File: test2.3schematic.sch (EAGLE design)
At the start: 24 parts, among them IC1 NCS21911SN2T1G, IC2 FXLN8371QR1, IC3 MAX25210ATAB9_V+, IC4 NCS21911SN2T1G, IC5 NCS21911SN2T1G

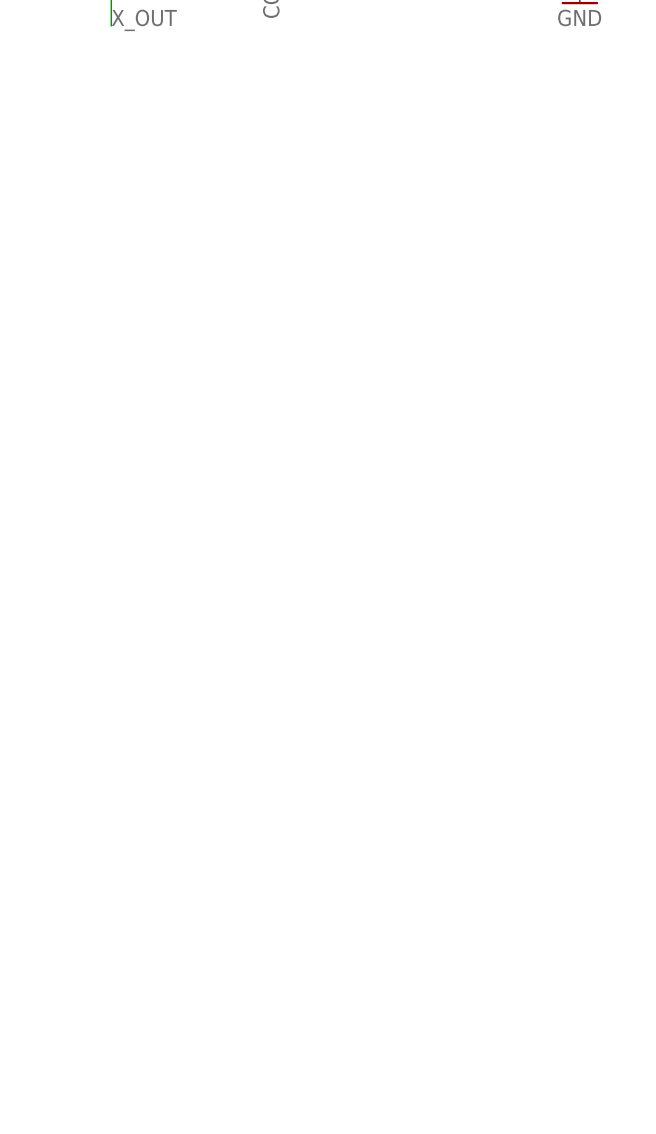
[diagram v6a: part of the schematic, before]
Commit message: FInal PCB, some parts might be bought using diff website if not PCB will be revised for later deadline
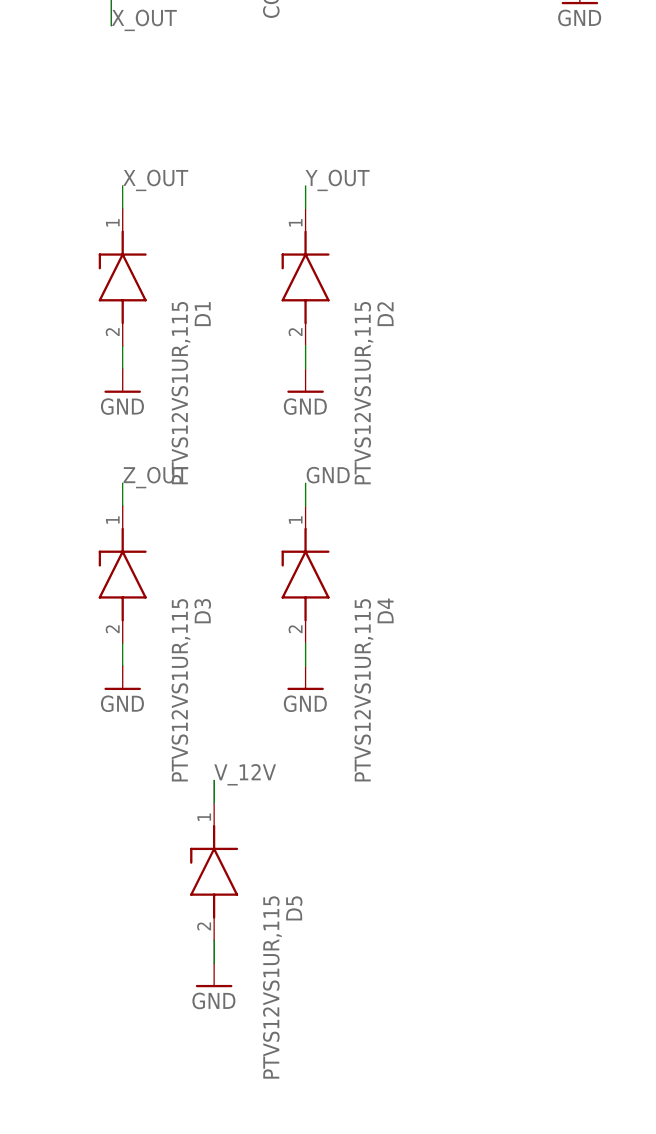
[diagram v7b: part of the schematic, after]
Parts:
- added D1, D2, D3, D4, D5: PTVS12VS1UR,115, SamacSys_Parts:PTVS12VS1UR,115
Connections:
- net GND: now also D1.A, D2.A, D3.A, D4.A, D4.K, D5.A
- net V_12V: now also D5.K
- net X_OUT: now also D1.K
- net Y_OUT: now also D2.K
- net Z_OUT: now also D3.K
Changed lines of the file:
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@@
 <part name="C11" library="SamacSys_Parts" library_urn="urn:adsk.eagle:library:32027058" deviceset="CNA6P1X7R1H475K250AE" device="" package3d_urn="urn:adsk.eagle:package:31985600/2"/>
 <part name="GND25" library="supply1" library_urn="urn:adsk.eagle:library:371" deviceset="GND" device=""/>
+<part name="D1" library="SamacSys_Parts" deviceset="PTVS12VS1UR,115" device=""/>
+<part name="D2" library="SamacSys_Parts" deviceset="PTVS12VS1UR,115" device=""/>
+<part name="D3" library="SamacSys_Parts" deviceset="PTVS12VS1UR,115" device=""/>
+<part name="D4" library="SamacSys_Parts" deviceset="PTVS12VS1UR,115" device=""/>
+<part name="D5" library="SamacSys_Parts" deviceset="PTVS12VS1UR,115" device=""/>
+<part name="GND26" library="supply1" library_urn="urn:adsk.eagle:library:371" deviceset="GND" device=""/>
+<part name="GND27" library="supply1" library_urn="urn:adsk.eagle:library:371" deviceset="GND" device=""/>
+<part name="GND28" library="supply1" library_urn="urn:adsk.eagle:library:371" deviceset="GND" device=""/>
+<part name="GND29" library="supply1" library_urn="urn:adsk.eagle:library:371" deviceset="GND" device=""/>
+<part name="GND30" library="supply1" library_urn="urn:adsk.eagle:library:371" deviceset="GND" device=""/>
 </parts>
 <sheets>
@@
 <attribute name="VALUE" x="-58.42" y="-33.02" size="1.778" layer="96"/>
 </instance>
+<instance part="D1" gate="G$1" x="-106.68" y="-53.34" smashed="yes" rot="R270">
+<attribute name="NAME" x="-97.79" y="-63.5" size="1.778" layer="95" rot="R270" align="center-left"/>
+<attribute name="VALUE" x="-100.33" y="-63.5" size="1.778" layer="96" rot="R270" align="center-left"/>
+</instance>
+<instance part="D2" gate="G$1" x="-86.36" y="-53.34" smashed="yes" rot="R270">
+<attribute name="NAME" x="-77.47" y="-63.5" size="1.778" layer="95" rot="R270" align="center-left"/>
+<attribute name="VALUE" x="-80.01" y="-63.5" size="1.778" layer="96" rot="R270" align="center-left"/>
+</instance>
+<instance part="D3" gate="G$1" x="-106.68" y="-86.36" smashed="yes" rot="R270">
+<attribute name="NAME" x="-97.79" y="-96.52" size="1.778" layer="95" rot="R270" align="center-left"/>
+<attribute name="VALUE" x="-100.33" y="-96.52" size="1.778" layer="96" rot="R270" align="center-left"/>
+</instance>
+<instance part="D4" gate="G$1" x="-86.36" y="-86.36" smashed="yes" rot="R270">
+<attribute name="NAME" x="-77.47" y="-96.52" size="1.778" layer="95" rot="R270" align="center-left"/>
+<attribute name="VALUE" x="-80.01" y="-96.52" size="1.778" layer="96" rot="R270" align="center-left"/>
+</instance>
+<instance part="D5" gate="G$1" x="-96.52" y="-119.38" smashed="yes" rot="R270">
+<attribute name="NAME" x="-87.63" y="-129.54" size="1.778" layer="95" rot="R270" align="center-left"/>
+<attribute name="VALUE" x="-90.17" y="-129.54" size="1.778" layer="96" rot="R270" align="center-left"/>
+</instance>
+<instance part="GND26" gate="1" x="-106.68" y="-73.66" smashed="yes">
+<attribute name="VALUE" x="-109.22" y="-76.2" size="1.778" layer="96"/>
+</instance>
+<instance part="GND27" gate="1" x="-86.36" y="-73.66" smashed="yes">
+<attribute name="VALUE" x="-88.9" y="-76.2" size="1.778" layer="96"/>
+</instance>
+<instance part="GND28" gate="1" x="-106.68" y="-106.68" smashed="yes">
+<attribute name="VALUE" x="-109.22" y="-109.22" size="1.778" layer="96"/>
+</instance>
+<instance part="GND29" gate="1" x="-86.36" y="-106.68" smashed="yes">
+<attribute name="VALUE" x="-88.9" y="-109.22" size="1.778" layer="96"/>
+</instance>
+<instance part="GND30" gate="1" x="-96.52" y="-139.7" smashed="yes">
+<attribute name="VALUE" x="-99.06" y="-142.24" size="1.778" layer="96"/>
+</instance>
 </instances>
 <busses>
@@
 <pinref part="GND25" gate="1" pin="GND"/>
 <wire x1="-55.88" y1="-20.32" x2="-55.88" y2="-27.94" width="0.1524" layer="91"/>
+</segment>
+<segment>
+<pinref part="D1" gate="G$1" pin="A"/>
+<wire x1="-106.68" y1="-68.58" x2="-106.68" y2="-71.12" width="0.1524" layer="91"/>
+<pinref part="GND26" gate="1" pin="GND"/>
+</segment>
+<segment>
+<pinref part="D2" gate="G$1" pin="A"/>
+<wire x1="-86.36" y1="-68.58" x2="-86.36" y2="-71.12" width="0.1524" layer="91"/>
+<pinref part="GND27" gate="1" pin="GND"/>
+</segment>
+<segment>
+<pinref part="D3" gate="G$1" pin="A"/>
+<wire x1="-106.68" y1="-101.6" x2="-106.68" y2="-104.14" width="0.1524" layer="91"/>
+<pinref part="GND28" gate="1" pin="GND"/>
+</segment>
+<segment>
+<pinref part="D4" gate="G$1" pin="A"/>
+<wire x1="-86.36" y1="-101.6" x2="-86.36" y2="-104.14" width="0.1524" layer="91"/>
+<pinref part="GND29" gate="1" pin="GND"/>
+</segment>
+<segment>
+<pinref part="D5" gate="G$1" pin="A"/>
+<wire x1="-96.52" y1="-134.62" x2="-96.52" y2="-137.16" width="0.1524" layer="91"/>
+<pinref part="GND30" gate="1" pin="GND"/>
+</segment>
+<segment>
+<pinref part="D4" gate="G$1" pin="K"/>
+<wire x1="-86.36" y1="-86.36" x2="-86.36" y2="-83.82" width="0.1524" layer="91"/>
+<label x="-86.36" y="-83.82" size="1.778" layer="95"/>
 </segment>
 </net>
@@
 <wire x1="177.8" y1="-77.47" x2="177.8" y2="-76.2" width="0.1524" layer="91"/>
 <junction x="177.8" y="-76.2"/>
+</segment>
+<segment>
+<pinref part="D5" gate="G$1" pin="K"/>
+<wire x1="-96.52" y1="-119.38" x2="-96.52" y2="-116.84" width="0.1524" layer="91"/>
+<label x="-96.52" y="-116.84" size="1.778" layer="95"/>
 </segment>
 </net>
@@
 <wire x1="-107.95" y1="-10.16" x2="-114.3" y2="-10.16" width="0.1524" layer="91"/>
 </segment>
+<segment>
+<pinref part="D1" gate="G$1" pin="K"/>
+<wire x1="-106.68" y1="-53.34" x2="-106.68" y2="-50.8" width="0.1524" layer="91"/>
+<label x="-106.68" y="-50.8" size="1.778" layer="95"/>
+</segment>
 </net>
 <net name="Y_OUT" class="0">
@@
 <label x="157.48" y="-2.54" size="1.778" layer="95"/>
 </segment>
+<segment>
+<pinref part="D2" gate="G$1" pin="K"/>
+<wire x1="-86.36" y1="-53.34" x2="-86.36" y2="-50.8" width="0.1524" layer="91"/>
+<label x="-86.36" y="-50.8" size="1.778" layer="95"/>
+</segment>
 </net>
 <net name="Z_OUT" class="0">
@@
 <wire x1="-105.41" y1="-5.08" x2="-114.3" y2="-5.08" width="0.1524" layer="91"/>
 </segment>
-</net>
+<segment>
+<pinref part="D3" gate="G$1" pin="K"/>
+<wire x1="-106.68" y1="-86.36" x2="-106.68" y2="-83.82" width="0.1524" layer="91"/>
+<label x="-106.68" y="-83.82" size="1.778" layer="95"/>
+</segment>
+</net>
